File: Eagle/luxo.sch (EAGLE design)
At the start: 2 parts

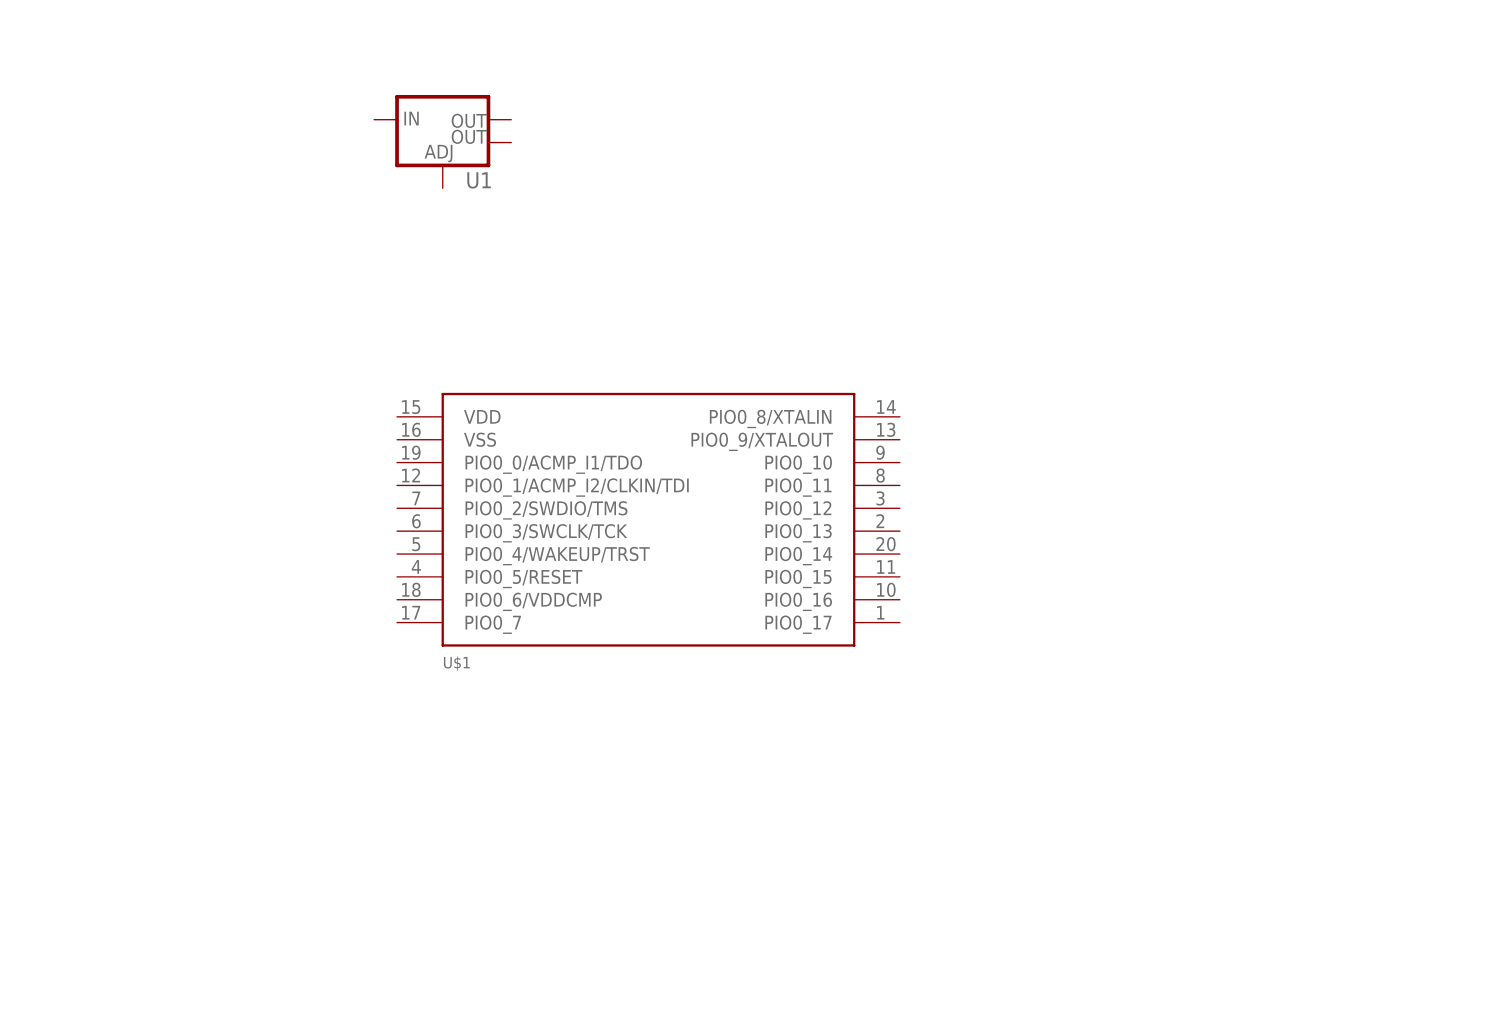
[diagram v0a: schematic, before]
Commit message: Add voltage regulator to schematic
Added 3.3v voltage regulator and 2 switches needed for LPC812 flashing.
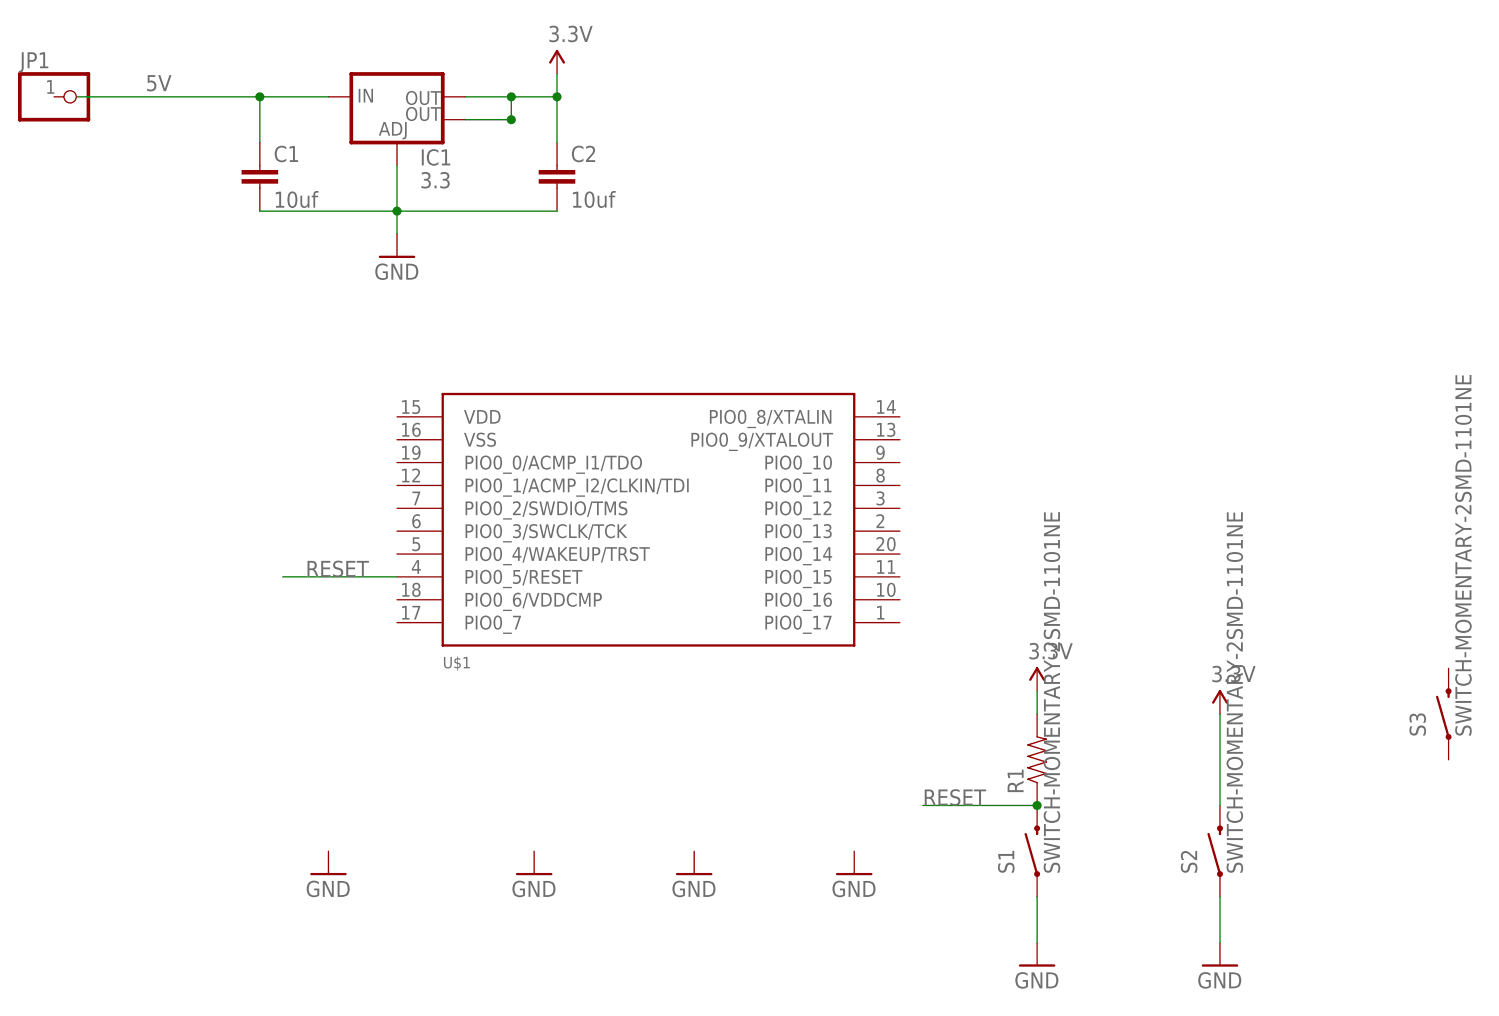
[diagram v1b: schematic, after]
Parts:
- removed U1: (no value), SparkFun-PowerIC:V_REG_LM1117SOT223
- added C1, C2: 10uf, SparkFun-Capacitors:10UF10V10%(0805)
- added IC1: 3.3, SparkFun-PowerIC:V_REG_LM1117SOT223
- added JP1: (no value), adafruit:PINHD-1X1
- added R1: (no value), SparkFun-Resistors:RESISTOR0805-RES
- added S1, S2, S3: SWITCH-MOMENTARY-2SMD-1101NE, SparkFun-Electromechanical:SWITCH-MOMENTARY-2SMD-1101NE
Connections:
- new net 3.3V: C2.1, IC1.OUT, IC1.OUT@1, R1.2, S2.2
- new net 5V: C1.1, IC1.IN
- new net GND: C1.2, C2.2, IC1.ADJ, S1.1, S2.1
- new net RESET: R1.1, S1.2, U$1.PIO0_5/RESET
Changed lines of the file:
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@@
 <layer number="230" name="230bmp" color="7" fill="1" visible="yes" active="yes"/>
 <layer number="231" name="231bmp" color="7" fill="1" visible="yes" active="yes"/>
+<layer number="232" name="Eagle3D_PG2" color="7" fill="1" visible="no" active="no"/>
+<layer number="233" name="Eagle3D_PG3" color="7" fill="1" visible="no" active="no"/>
 <layer number="248" name="Housing" color="7" fill="1" visible="yes" active="yes"/>
 <layer number="249" name="Edge" color="7" fill="1" visible="yes" active="yes"/>
@@
 <parts>
 <part name="U$1" library="LPC800" deviceset="LPC812M101JDH20" device=""/>
-<part name="U1" library="SparkFun-PowerIC" deviceset="V_REG_LM1117" device="SOT223"/>
+<part name="IC1" library="SparkFun-PowerIC" deviceset="V_REG_LM1117" device="SOT223" value="3.3"/>
+<part name="C1" library="SparkFun-Capacitors" deviceset="10UF10V10%(0805)" device="" value="10uf"/>
+<part name="C2" library="SparkFun-Capacitors" deviceset="10UF10V10%(0805)" device="" value="10uf"/>
+<part name="GND1" library="SparkFun-Aesthetics" deviceset="GND" device=""/>
+<part name="GND2" library="SparkFun-Aesthetics" deviceset="GND" device=""/>
+<part name="GND3" library="SparkFun-Aesthetics" deviceset="GND" device=""/>
+<part name="GND4" library="SparkFun-Aesthetics" deviceset="GND" device=""/>
+<part name="GND5" library="SparkFun-Aesthetics" deviceset="GND" device=""/>
+<part name="GND6" library="SparkFun-Aesthetics" deviceset="GND" device=""/>
+<part name="GND7" library="SparkFun-Aesthetics" deviceset="GND" device=""/>
+<part name="SUPPLY1" library="SparkFun-Aesthetics" deviceset="3.3V" device=""/>
+<part name="JP1" library="adafruit" deviceset="PINHD-1X1" device=""/>
+<part name="S1" library="SparkFun-Electromechanical" deviceset="SWITCH-MOMENTARY-2" device="SMD-1101NE"/>
+<part name="S2" library="SparkFun-Electromechanical" deviceset="SWITCH-MOMENTARY-2" device="SMD-1101NE"/>
+<part name="S3" library="SparkFun-Electromechanical" deviceset="SWITCH-MOMENTARY-2" device="SMD-1101NE"/>
+<part name="SUPPLY2" library="SparkFun-Aesthetics" deviceset="3.3V" device=""/>
+<part name="SUPPLY3" library="SparkFun-Aesthetics" deviceset="3.3V" device=""/>
+<part name="R1" library="SparkFun-Resistors" deviceset="RESISTOR" device="0805-RES"/>
 </parts>
 <sheets>
@@
 <instances>
 <instance part="U$1" gate="G$1" x="58.42" y="40.64"/>
-<instance part="U1" gate="G$1" x="35.56" y="86.36"/>
+<instance part="IC1" gate="G$1" x="30.48" y="88.9"/>
+<instance part="C1" gate="G$1" x="15.24" y="78.74"/>
+<instance part="C2" gate="G$1" x="48.26" y="78.74"/>
+<instance part="GND1" gate="1" x="30.48" y="71.12"/>
+<instance part="GND2" gate="1" x="81.28" y="2.54"/>
+<instance part="GND3" gate="1" x="101.6" y="-7.62"/>
+<instance part="GND4" gate="1" x="121.92" y="-7.62"/>
+<instance part="GND5" gate="1" x="63.5" y="2.54"/>
+<instance part="GND6" gate="1" x="45.72" y="2.54"/>
+<instance part="GND7" gate="1" x="22.86" y="2.54"/>
+<instance part="SUPPLY1" gate="G$1" x="48.26" y="91.44"/>
+<instance part="JP1" gate="G$1" x="-5.08" y="88.9"/>
+<instance part="S1" gate="G$1" x="101.6" y="5.08" rot="R90"/>
+<instance part="S2" gate="G$1" x="121.92" y="5.08" rot="R90"/>
+<instance part="S3" gate="G$1" x="147.32" y="20.32" rot="R90"/>
+<instance part="SUPPLY2" gate="G$1" x="101.6" y="22.86"/>
+<instance part="SUPPLY3" gate="G$1" x="121.92" y="20.32"/>
+<instance part="R1" gate="G$1" x="101.6" y="15.24" rot="R90"/>
 </instances>
 <busses>
 </busses>
 <nets>
+<net name="GND" class="0">
+<segment>
+<pinref part="GND1" gate="1" pin="GND"/>
+<wire x1="30.48" y1="73.66" x2="30.48" y2="76.2" width="0.1524" layer="91"/>
+<pinref part="C2" gate="G$1" pin="2"/>
+<wire x1="48.26" y1="76.2" x2="30.48" y2="76.2" width="0.1524" layer="91"/>
+<pinref part="C1" gate="G$1" pin="2"/>
+<pinref part="IC1" gate="G$1" pin="ADJ"/>
+<wire x1="15.24" y1="76.2" x2="30.48" y2="76.2" width="0.1524" layer="91"/>
+<wire x1="30.48" y1="76.2" x2="30.48" y2="81.28" width="0.1524" layer="91"/>
+<junction x="30.48" y="76.2"/>
+</segment>
+<segment>
+<pinref part="GND3" gate="1" pin="GND"/>
+<pinref part="S1" gate="G$1" pin="1"/>
+<wire x1="101.6" y1="-5.08" x2="101.6" y2="0" width="0.1524" layer="91"/>
+</segment>
+<segment>
+<pinref part="GND4" gate="1" pin="GND"/>
+<pinref part="S2" gate="G$1" pin="1"/>
+<wire x1="121.92" y1="-5.08" x2="121.92" y2="0" width="0.1524" layer="91"/>
+</segment>
+</net>
+<net name="5V" class="0">
+<segment>
+<pinref part="IC1" gate="G$1" pin="IN"/>
+<wire x1="22.86" y1="88.9" x2="15.24" y2="88.9" width="0.1524" layer="91"/>
+<pinref part="C1" gate="G$1" pin="1"/>
+<wire x1="15.24" y1="88.9" x2="15.24" y2="83.82" width="0.1524" layer="91"/>
+<wire x1="15.24" y1="88.9" x2="-5.08" y2="88.9" width="0.1524" layer="91"/>
+<junction x="15.24" y="88.9"/>
+<label x="2.54" y="89.535" size="1.778" layer="95"/>
+</segment>
+</net>
+<net name="3.3V" class="0">
+<segment>
+<pinref part="IC1" gate="G$1" pin="OUT@1"/>
+<wire x1="38.1" y1="86.36" x2="43.18" y2="86.36" width="0.1524" layer="91"/>
+<wire x1="43.18" y1="86.36" x2="43.18" y2="88.9" width="0.1524" layer="91"/>
+<pinref part="C2" gate="G$1" pin="1"/>
+<wire x1="48.26" y1="88.9" x2="48.26" y2="83.82" width="0.1524" layer="91"/>
+<pinref part="IC1" gate="G$1" pin="OUT"/>
+<wire x1="38.1" y1="88.9" x2="43.18" y2="88.9" width="0.1524" layer="91"/>
+<wire x1="43.18" y1="88.9" x2="48.26" y2="88.9" width="0.1524" layer="91"/>
+<wire x1="48.26" y1="88.9" x2="48.26" y2="91.44" width="0.1524" layer="91"/>
+<junction x="48.26" y="88.9"/>
+<junction x="43.18" y="88.9"/>
+<junction x="43.18" y="86.36"/>
+<pinref part="SUPPLY1" gate="G$1" pin="3.3V"/>
+</segment>
+<segment>
+<pinref part="S2" gate="G$1" pin="2"/>
+<pinref part="SUPPLY3" gate="G$1" pin="3.3V"/>
+<wire x1="121.92" y1="10.16" x2="121.92" y2="20.32" width="0.1524" layer="91"/>
+</segment>
+<segment>
+<pinref part="SUPPLY2" gate="G$1" pin="3.3V"/>
+<pinref part="R1" gate="G$1" pin="2"/>
+<wire x1="101.6" y1="22.86" x2="101.6" y2="20.32" width="0.1524" layer="91"/>
+</segment>
+</net>
+<net name="RESET" class="0">
+<segment>
+<pinref part="S1" gate="G$1" pin="2"/>
+<wire x1="101.6" y1="10.16" x2="88.9" y2="10.16" width="0.1524" layer="91"/>
+<pinref part="R1" gate="G$1" pin="1"/>
+<junction x="101.6" y="10.16"/>
+<label x="88.9" y="10.16" size="1.778" layer="95"/>
+</segment>
+<segment>
+<pinref part="U$1" gate="G$1" pin="PIO0_5/RESET"/>
+<wire x1="30.48" y1="35.56" x2="17.78" y2="35.56" width="0.1524" layer="91"/>
+<label x="20.32" y="35.56" size="1.778" layer="95"/>
+</segment>
+</net>
 </nets>
 </sheet>

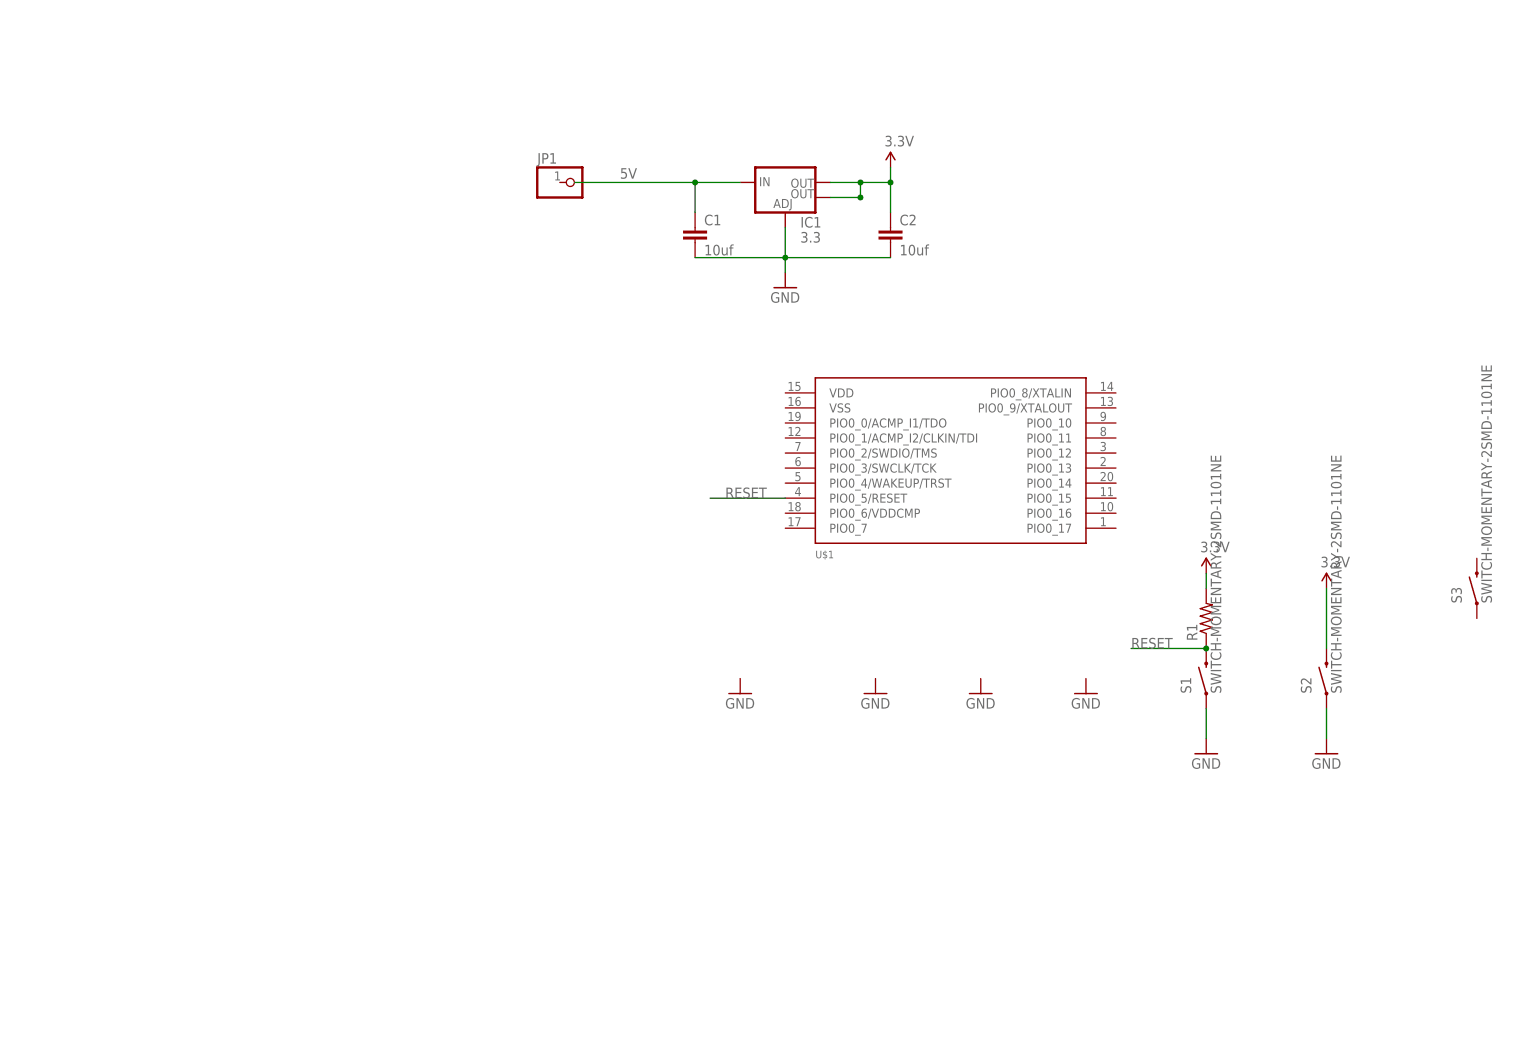
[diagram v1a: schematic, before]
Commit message: Add logic level shifter
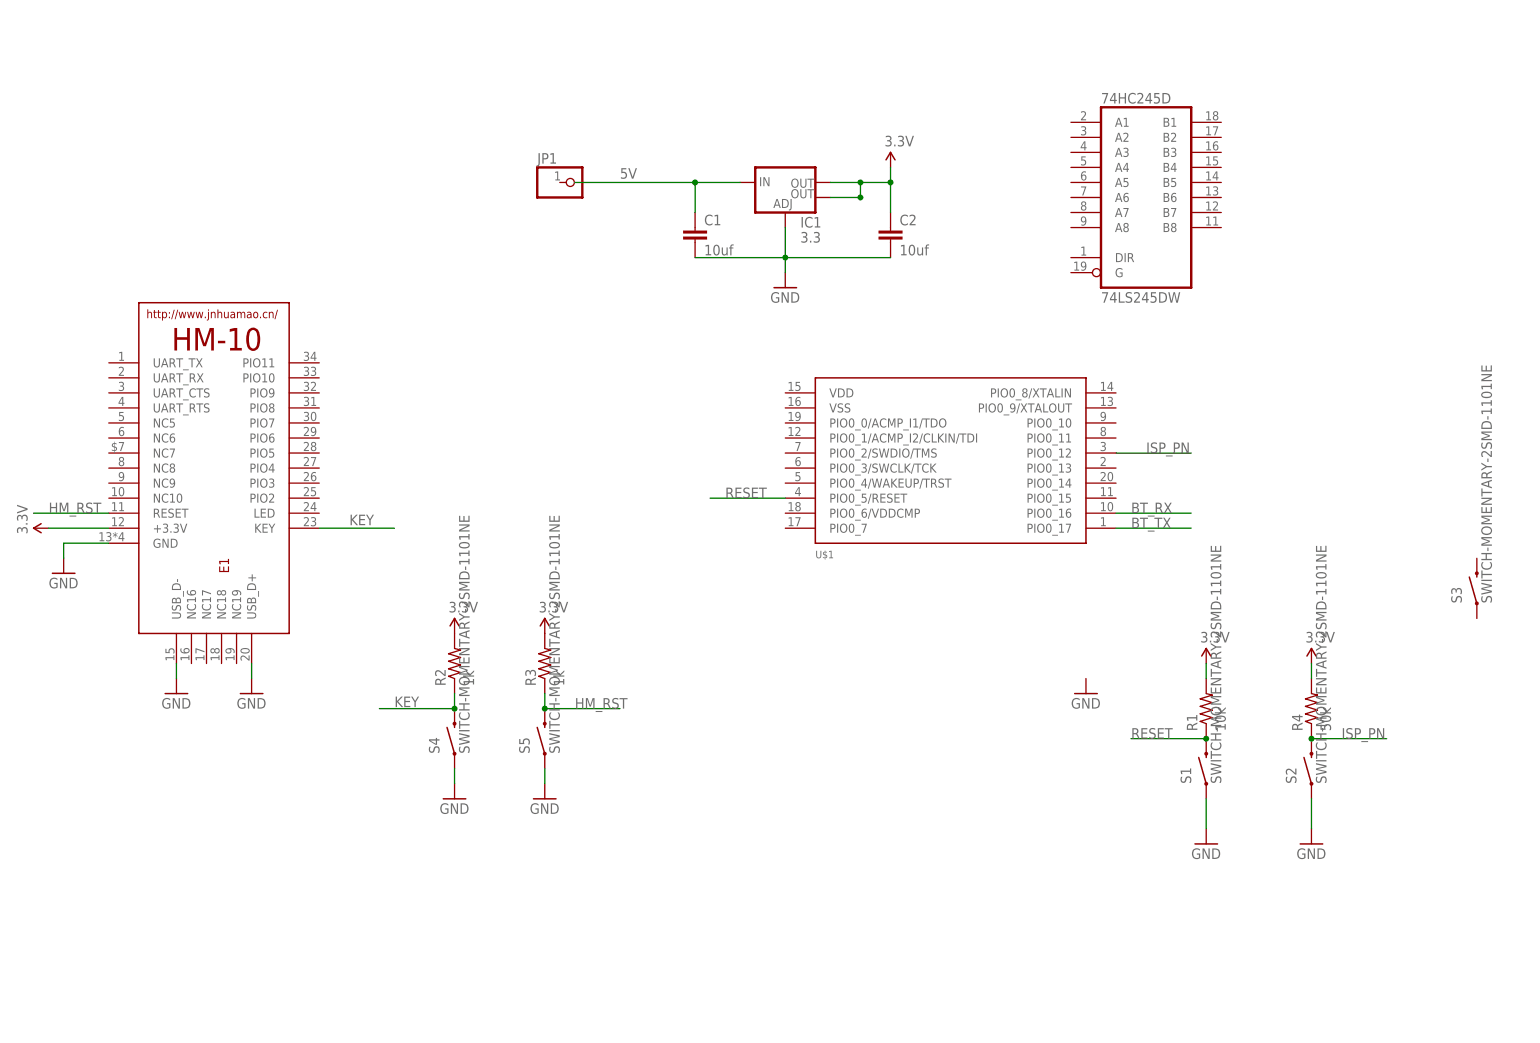
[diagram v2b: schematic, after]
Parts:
- added 74HC245D: 74LS245DW, 74xx-us:74LS245DW
- added E1: HM-10-BOARD, JNHuaMao:HM-10-BOARD
- added R2, R3: 1k, SparkFun-Resistors:RESISTOR0805-RES
- added R4: 50k, SparkFun-Resistors:RESISTOR0805-RES
- added S4, S5: SWITCH-MOMENTARY-2SMD-1101NE, SparkFun-Electromechanical:SWITCH-MOMENTARY-2SMD-1101NE
- R1: value (none) -> 10k
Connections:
- new net BT_RX: U$1.PIO0_16
- new net BT_TX: U$1.PIO0_17
- new net HM_RST: E1.RESET, R3.1, S5.2
- new net ISP_PN: R4.1, S2.2, U$1.PIO0_12
- new net KEY: E1.KEY, R2.1, S4.2
- net 3.3V: now also E1.+3.3V, R2.2, R3.2, R4.2; no longer S2.2
- net GND: now also E1.GND, S4.1, S5.1
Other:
- moved on the sheet: R1, S1, S2
